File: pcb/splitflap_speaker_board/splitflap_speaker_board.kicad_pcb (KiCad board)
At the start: 4 copper layers, 130 x 75 mm, 81 parts, among them J14 L_out, J15 R_out, J8 POT, Q1 BSS138, Q2 BSS138, U1 TPS562243DRLR, U2 LM1084-5.0, U3 PCM5122PW, U4 MAX9744

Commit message: Fix speaker board blockers and match software to the board pins
Board + schematic (kept in sync; netlists now match pad for pad):
- Buck feedback R7 100k -> 10k so the "+7V" rail is 6.6 V, not 1.2 V
- PCM5122: AVDD tied to +3.3V; SCK grounded; MODE2 grounded for
  hardware mode with ATT1/ATT2/AGNS grounded (0 dB, 2 Vrms)
- MAX9744 analog volume mode: slide pot wiper on SDA/VOL, SCLK to GND
  (filterless); amp taken off the I2C bus
- MAX9744 exposed pad + thermal vias on GND (EP pin added to symbol)
- Left channel input/feedback resistors moved to the correct pins
- LED strip data moved from GPIO5 to GPIO10 (SPI0 MOSI)
- C15/C16 (2.2 uF straight on the DAC outputs) marked DNP
- Schematic: connector refs, Pi socket and L1/C4/C28 footprints and
  J14 pin order updated to match the board; speaker +/- silk moved
  next to the terminals

Software:
- Replace I2C amp driver and ADS1115 pot reader with GPIO control of
  DAC XSMT/ATT0/MAST/FLT and amp SHDN/MUTE
- Web volume slider now sets MPD stream volume
- Buttons on GPIO0 (snooze) and GPIO12 (LED); docs updated for the
  Pi Zero W and the hifiberry-dac overlay

Zone fills were not regenerated: refill zones in KiCad before DRC/plots.

Co-Authored-By: Claude Opus 5.5 <noreply@anthropic.com>
Claude-Session: https://claude.ai/code/session_01FgEhnNNRCVfH3GgykTypvy
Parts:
- R7: value 100k_0603 -> 10k
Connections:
- C12 pad 2: /AVDD -> +3.3V
- C14 pad 1: /AVDD -> +3.3V
- R10 pad 1: /INL -> /FBL
- R10 pad 2: /FBL -> /INL
- Raspberry pad 19: /GP8 -> /LED
- Raspberry pad 29: /LED -> unconnected-(J6-Pin_29-Pad29)
- U3 pad 11: /POT_IN -> GND
- U3 pad 12: unconnected-(U3-SCL/MC/ATT1-Pad12) -> GND
- U3 pad 15: unconnected-(U3-GPIO3/AGNS-Pad15) -> GND
- U3 pad 18: +3.3V -> GND
- U3 pad 20: /DGND -> GND
- U3 pad 8: /AVDD -> +3.3V
- U4 pad 16: /FBL -> /INL
- U4 pad 17: /INL -> /FBL
- U4 pad 45: (no net) -> GND
- U4 pad 8: /SDA_3.3V -> /POT_IN
- U4 pad 9: /SCL_3.3V -> GND
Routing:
- net /SCL_3.3V: track 109.2 -> 66.1 mm, vias 7 -> 3
- net /SDA_3.3V: track 95.8 -> 57.2 mm, vias 4 -> 2
- net /POT_IN: track 84.0 -> 56.9 mm, vias 0 -> 2
- net GND: track 43.1 -> 60.3 mm, vias 40 -> 41
- net /LED: track 39.7 -> 52.6 mm, vias 0 -> 1
- net /AVDD: track 10.0 -> 0.00 mm
- net +3.3V: track 262.2 -> 257.7 mm, vias 5 -> 4
- net /INL: track 5.07 -> 9.01 mm, vias 0 -> 2
- net /FBL: track 4.49 -> 3.59 mm

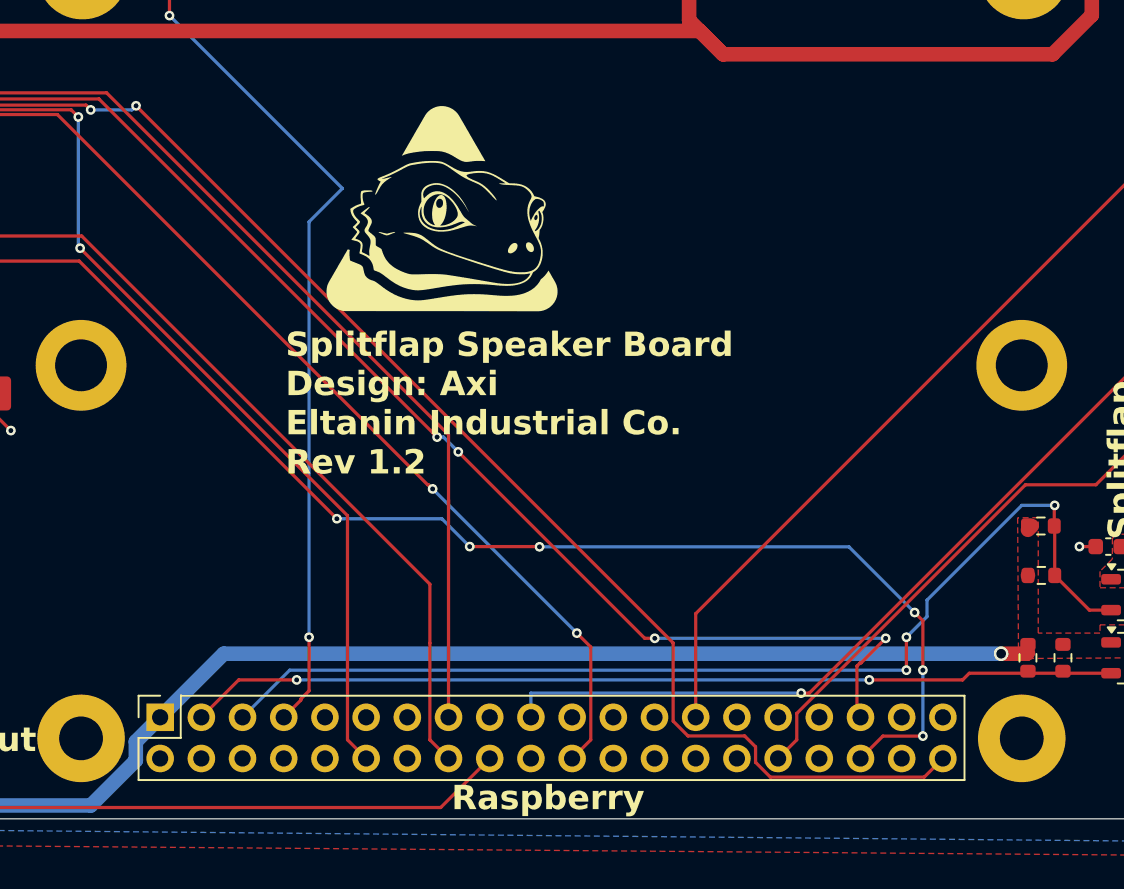
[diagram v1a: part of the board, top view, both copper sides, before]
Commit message: Mirror Pi socket for a face-up Pi Zero W and re-route the header
The Pi Zero W now mounts component side up with its header pins pointing
down into the board's socket. That mirrors the pinout, so:

- New footprint eltanin_footprints:PinSocket_2x20_P2.54mm_Vertical_PiFaceUp
  (stock 2x20 socket with mirrored pad numbering), pin 1 at the east end
- Re-routed 3.3 V, I2C, I2S (BCK/LRCK/DIN) and SPI MOSI to their new pins;
  5 V and GND reach the Pi through the inner planes as before
- GPIO signals moved to free pins: snooze GPIO27, LED button GPIO4,
  amp ~SHDN GPIO13, amp MUTE GPIO25
- DAC straps tied on the board instead of Pi GPIOs: XSMT high,
  MAST/ATT0/FLT low
- Schematic updated to match; software config and docs follow

Zone fills were not regenerated: refill zones in KiCad before DRC/plots.

Co-Authored-By: Claude Opus 5.5 <noreply@anthropic.com>
Claude-Session: https://claude.ai/code/session_01FgEhnNNRCVfH3GgykTypvy
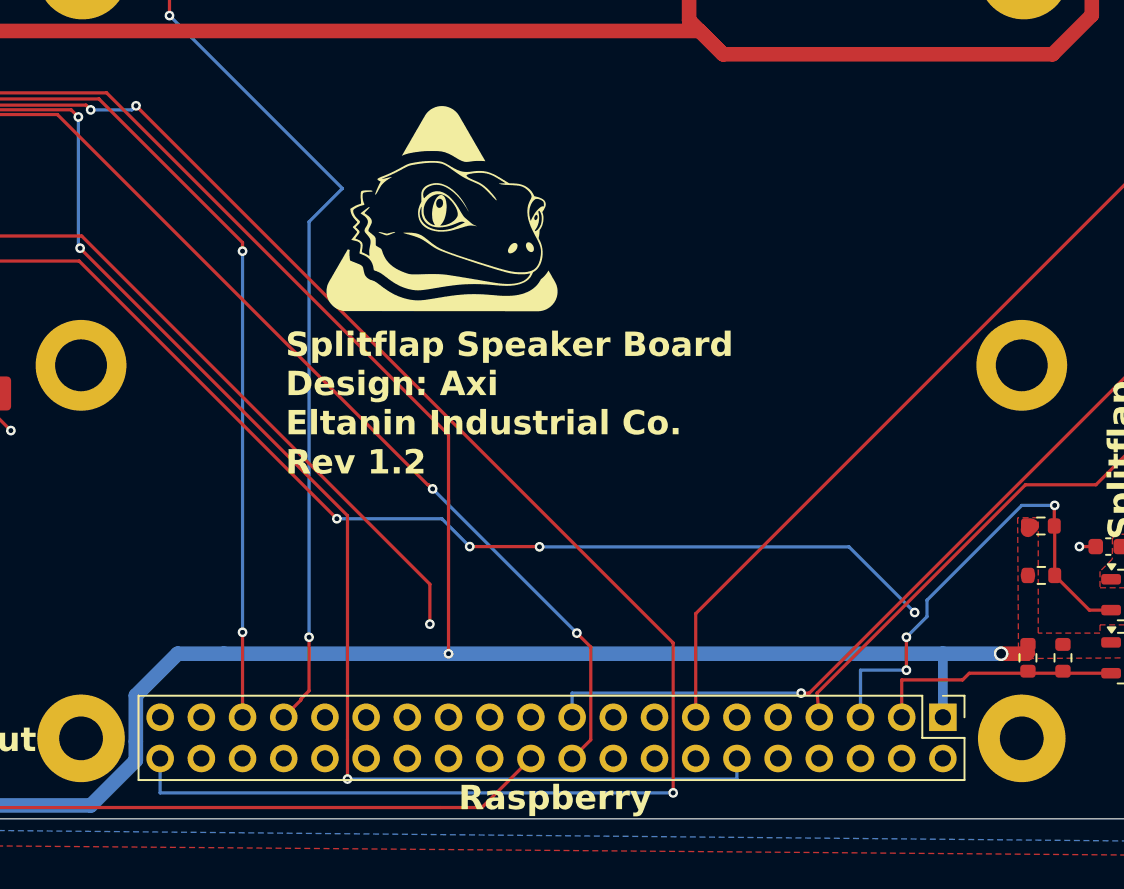
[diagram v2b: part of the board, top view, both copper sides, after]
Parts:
- Raspberry: footprint Connector_PinSocket_2.54mm:PinSocket_2x20_P2.54mm_Vertical -> eltanin_footprints:PinSocket_2x20_P2.54mm_Vertical_PiFaceUp
- moved Raspberry 48.3 mm to (214.3, 151.2)
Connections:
- Raspberry pad 13: unconnected-(J6-Pin_13-Pad13) -> /SNOOZE
- Raspberry pad 15: /GP3 -> unconnected-(J6-Pin_15-Pad15)
- Raspberry pad 16: /GP4 -> unconnected-(J6-Pin_16-Pad16)
- Raspberry pad 18: /MUTE -> unconnected-(J6-Pin_18-Pad18)
- Raspberry pad 22: /GP6 -> /MUTE
- Raspberry pad 27: /SNOOZE -> unconnected-(J6-Pin_27-Pad27)
- Raspberry pad 32: /ILLU -> unconnected-(J6-Pin_32-Pad32)
- Raspberry pad 33: unconnected-(J6-Pin_33-Pad33) -> /SHND
- Raspberry pad 36: /GP5 -> unconnected-(J6-Pin_36-Pad36)
- Raspberry pad 6: unconnected-(J6-Pin_6-Pad6) -> GND
- Raspberry pad 7: /SHND -> /ILLU
- U3 pad 13: /GP5 -> GND
- U3 pad 14: /GP4 -> GND
- U3 pad 19: /GP6 -> GND
- U3 pad 25: /GP3 -> +3.3V
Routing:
- net GND: track 60.3 -> 274.9 mm, vias 41 -> 48
- net /GP5: track 95.5 -> 0.00 mm, vias 6 -> 0
- net +3.3V: track 257.7 -> 337.9 mm, vias 4 -> 5
- net /GP3: track 78.6 -> 0.00 mm
- net /GP6: track 77.4 -> 0.00 mm, vias 2 -> 0
- net /GP4: track 62.8 -> 0.00 mm
- net /SDA_3.3V: track 57.2 -> 15.4 mm, vias 2 -> 0
- net /SCL_3.3V: track 66.1 -> 29.7 mm
- net /LRCK: track 97.1 -> 70.8 mm, vias 4 -> 2
- net /BCK: track 73.3 -> 99.4 mm, vias 2 -> 3
- net /DIN: track 102.5 -> 120.6 mm, vias 2 -> 3
- net /ILLU: track 60.3 -> 56.8 mm
- net /MUTE: track 105.2 -> 107.7 mm
- net /LED: track 52.6 -> 50.0 mm
